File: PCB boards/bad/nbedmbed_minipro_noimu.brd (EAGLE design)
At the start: 63.5 x 47 mm, 16 parts

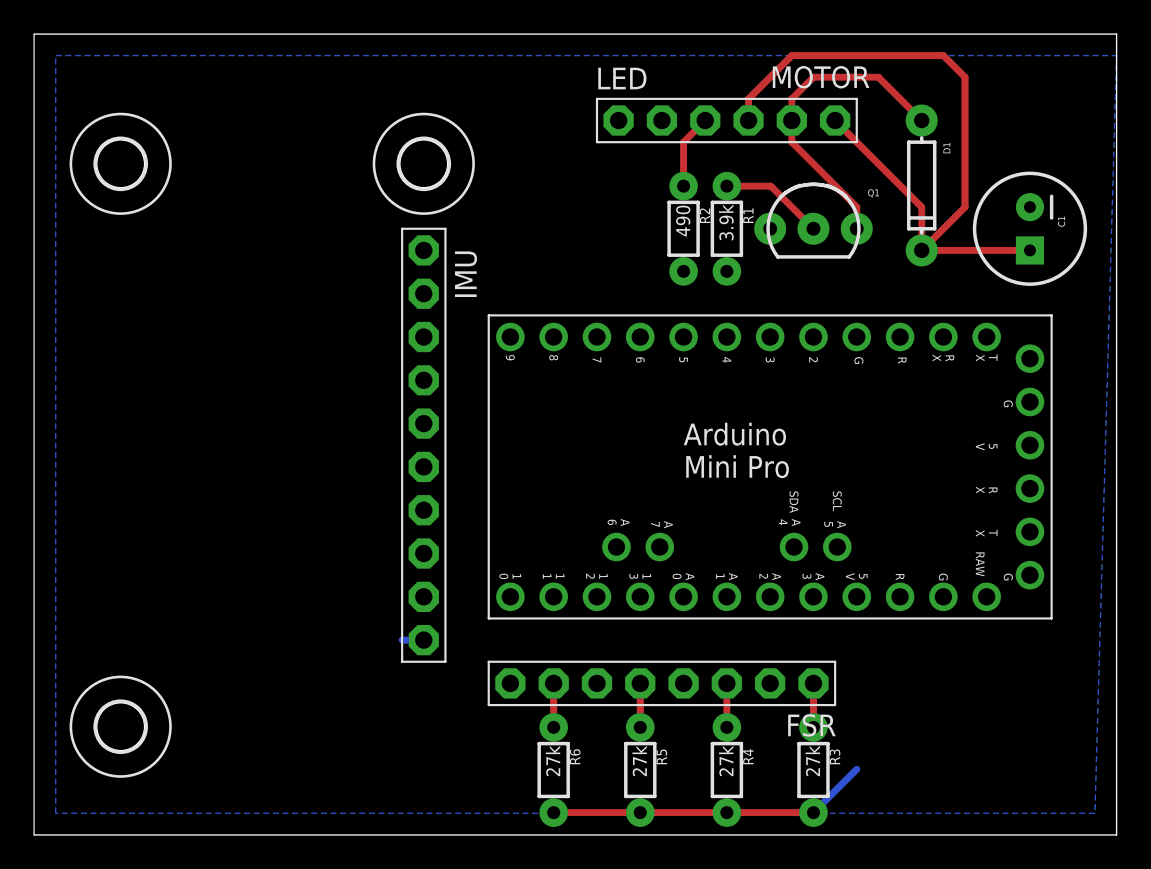
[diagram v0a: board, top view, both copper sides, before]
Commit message: updated arduino code
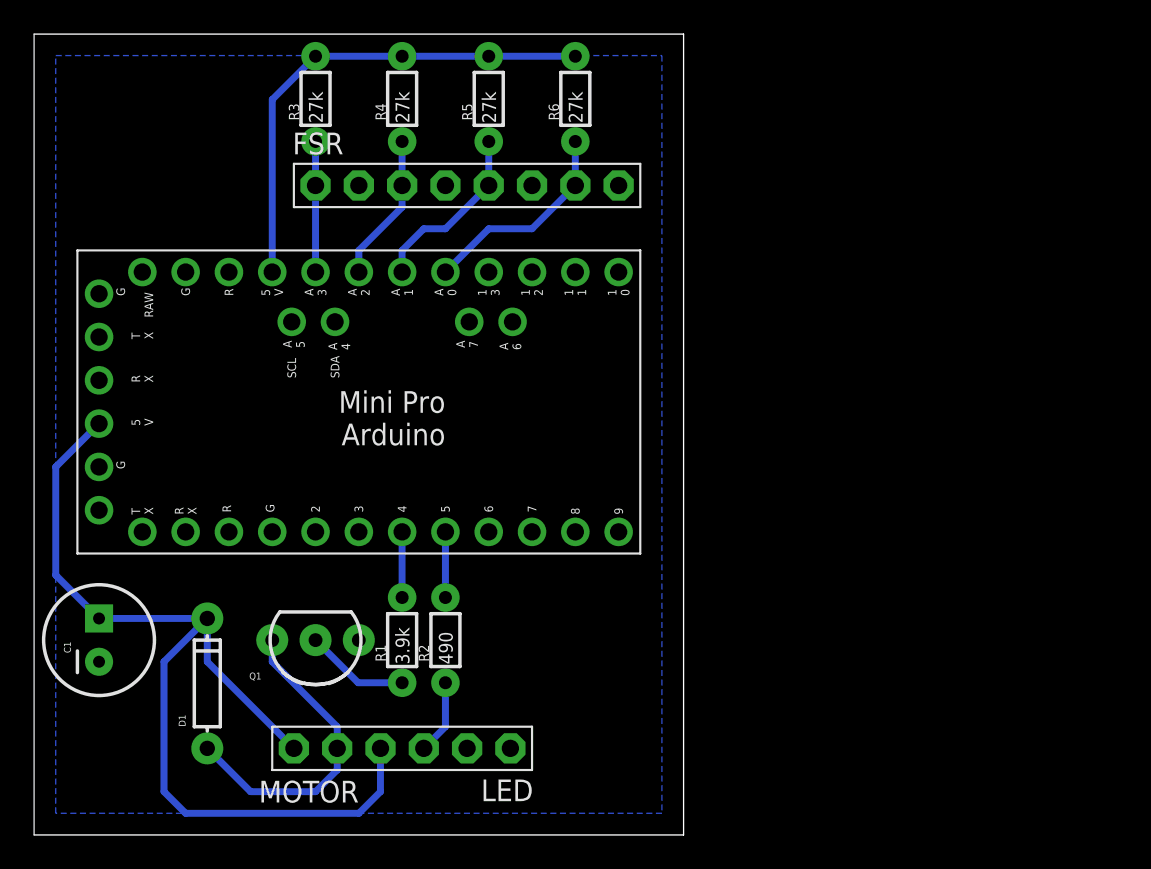
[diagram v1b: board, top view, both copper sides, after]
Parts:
- removed H1, H2, H3: MOUNT-HOLE2.8, holes:2,8
- removed IMU: 9D0F, adafruit:1X10-BIG
- moved C1 59.7 mm to (3.81, 11.4), turned to 90 degrees
- moved D1 51.1 mm to (10.2, 8.89), turned to 90 degrees
- moved R3 49.0 mm to (16.5, 43.2), turned to 90 degrees
- moved R4 43.7 mm to (21.6, 43.2), turned to 90 degrees
- moved LED 41.5 mm to (21.6, 5.08), turned to 180 degrees
- moved R5 40.4 mm to (26.7, 43.2), turned to 90 degrees
- moved R6 39.4 mm to (31.8, 43.2), turned to 90 degrees
- moved Q1 37.9 mm to (16.5, 11.4), turned to 180 degrees
- moved FSR 31.4 mm to (25.4, 38.1), turned to 0 degrees
- moved R1 30.7 mm to (21.6, 11.4), turned to 90 degrees
- moved R2 27.9 mm to (24.1, 11.4), turned to 90 degrees
- moved PCB2 23.3 mm to (35.6, 34.3), turned to 180 degrees
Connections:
- removed net N$10: IMU.6, PCB2.A4
- removed net N$11: IMU.7, PCB2.A5
- net FSR/IMU_5V: no longer IMU.10
- net GND: no longer IMU.8, PCB2...GND
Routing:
- net MOTOR/LED_5V: track 42.8 -> 57.1 mm
- net N$9: track 2.58 -> 12.3 mm
- net FSR/IMU_5V: track 20.1 -> 29.0 mm
- net N$8: track 2.58 -> 10.5 mm
- net N$6: track 2.58 -> 8.71 mm
- net N$5: track 2.58 -> 7.66 mm
- net N$2: track 0.00 -> 3.85 mm
- net N$1: track 0.00 -> 3.85 mm
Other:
- board size 63.5 x 47 mm -> 38.1 x 47 mm
